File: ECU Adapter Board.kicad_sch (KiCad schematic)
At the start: 4 parts

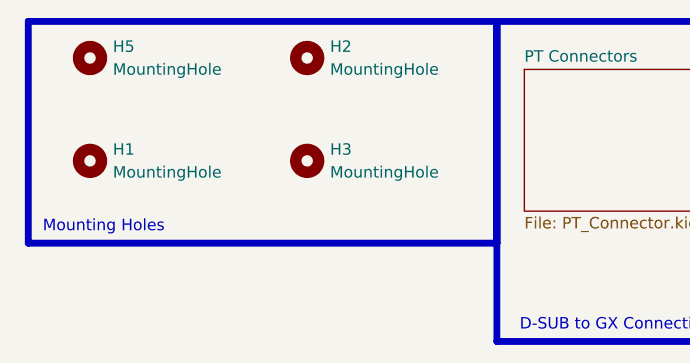
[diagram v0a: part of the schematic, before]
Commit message: grounded mounting holes
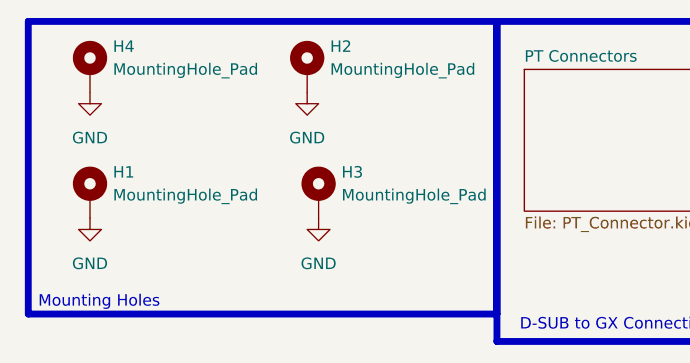
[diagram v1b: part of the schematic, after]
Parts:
- removed H1, H2, H3, H5: MountingHole, MountingHole:MountingHole_4.3mm_M4_Pad_Via, symbol Mechanical:MountingHole
- added H1, H2, H3, H4: MountingHole_Pad, MountingHole:MountingHole_4.3mm_M4_Pad_Via, symbol Mechanical:MountingHole_Pad
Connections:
- new net GND: H1.1, H2.1, H3.1, H4.1

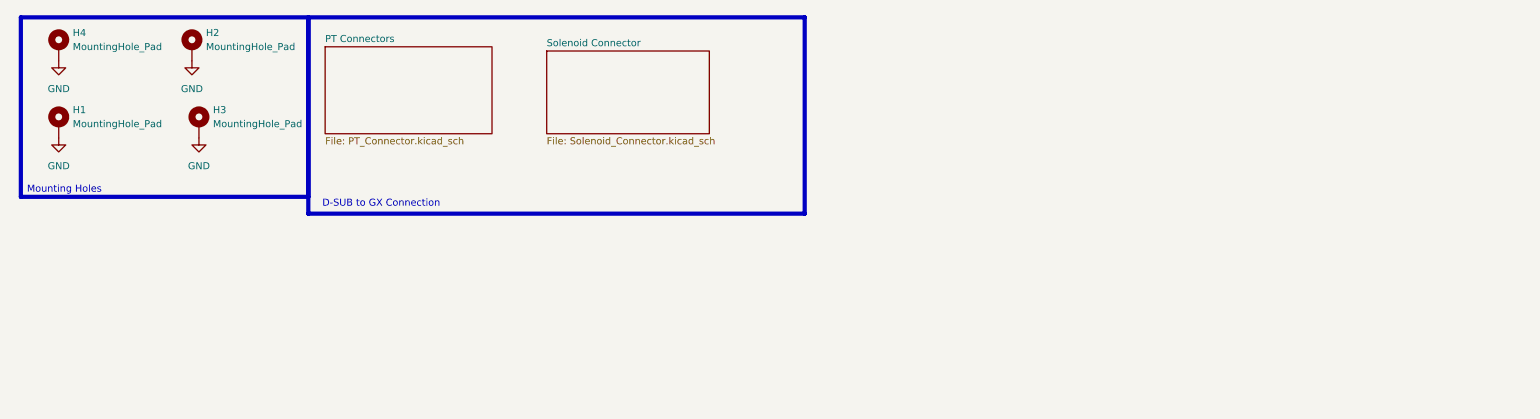
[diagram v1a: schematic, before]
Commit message: grounded pin 11 on PT Connectors
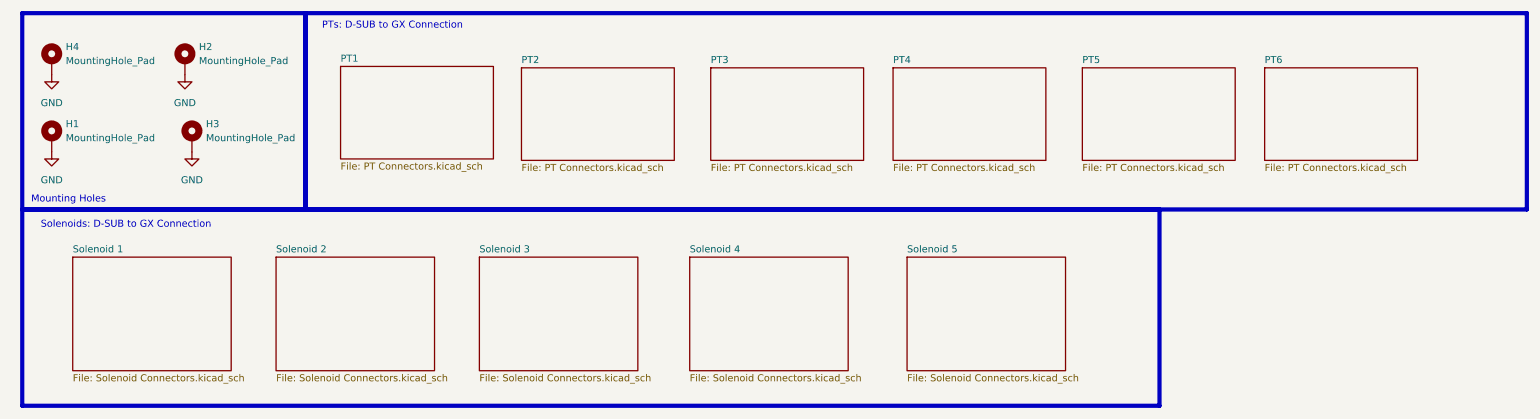
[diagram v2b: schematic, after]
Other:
- removed sheet PT Connectors
- removed sheet Solenoid Connector
- added sheet PT1 (PT Connectors.kicad_sch)
- added sheet PT2 (PT Connectors.kicad_sch)
- added sheet PT3 (PT Connectors.kicad_sch)
- added sheet PT4 (PT Connectors.kicad_sch)
- added sheet PT5 (PT Connectors.kicad_sch)
- added sheet PT6 (PT Connectors.kicad_sch)
- added sheet Solenoid 1 (Solenoid Connectors.kicad_sch)
- added sheet Solenoid 2 (Solenoid Connectors.kicad_sch)
- added sheet Solenoid 3 (Solenoid Connectors.kicad_sch)
- added sheet Solenoid 4 (Solenoid Connectors.kicad_sch)
- added sheet Solenoid 5 (Solenoid Connectors.kicad_sch)
- note added: "PTs: D-SUB to GX Connection"
- note added: "Solenoids: D-SUB to GX Connection"
- note removed: "D-SUB to GX Connection"
- moved on the sheet: H1, H2, H3, H4
